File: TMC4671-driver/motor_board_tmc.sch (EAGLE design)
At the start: 135 parts, among them U1 TMC4671-ES, U10 BSC030N08NS5ATMA1, U11 BSC030N08NS5ATMA1, U12 INA28X, U13 INA28X, U14 BSC030N08NS5ATMA1, U15 BSC030N08NS5ATMA1, U16 BSC030N08NS5ATMA1, U17 BSC030N08NS5ATMA1, U18 MCP14XX, U19 BSC030N08NS5ATMA1, U20 BSC030N08NS5ATMA1, U21 BSC030N08NS5ATMA1, U22 NC7NZ17K8X-3-BUFFER, U23 NC7NZ17K8X-3-BUFFER, U3 LM5109BSD, U4 LM5109BSD, U5 LM5109BSD, U6 LM5109BSD, U7 AP3012KTR-G1, U8 LM5050Q1MK-1/NOPB, U9 BSC030N08NS5ATMA1, X1 GMSTBA4, X2 GMSTBA4, X3 2516-, Y1 ECS-327KE-TR

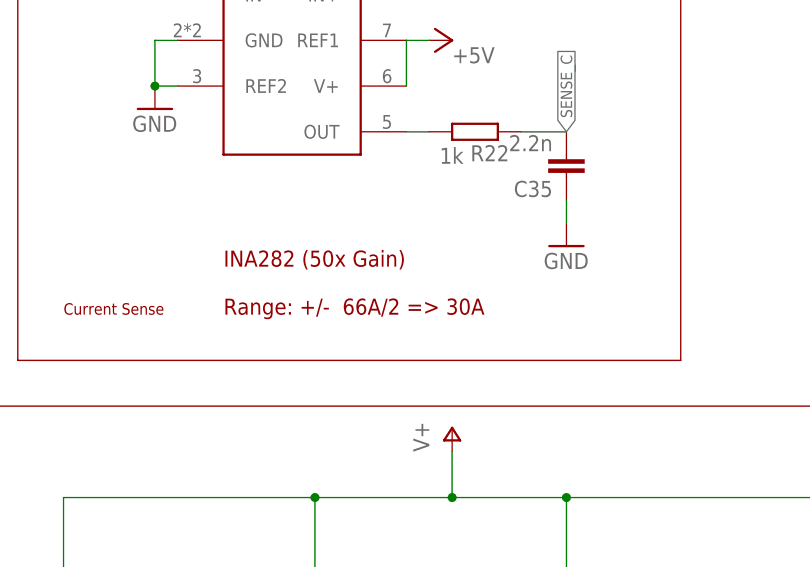
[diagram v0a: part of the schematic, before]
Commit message: Changing clearances to 8 mil and renamed shunt amps
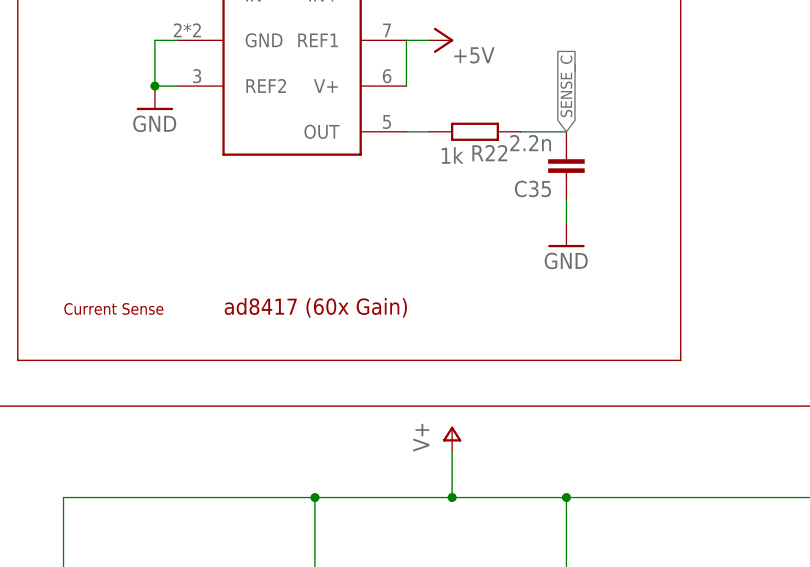
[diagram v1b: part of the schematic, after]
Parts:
- U12, U13: value INA28X -> AD841X; device Powermisc:INA28X -> Powermisc:AD841X
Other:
- note added: "ad8417 (60x Gain)"
- note removed: "INA282 (50x Gain) Range: +/- 66A/2 => 30A"
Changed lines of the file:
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@@
 <part name="R20" library="resistor" library_urn="urn:adsk.eagle:library:348" deviceset="R-EU_" device="R2512" package3d_urn="urn:adsk.eagle:package:23545/2" value="1.5m"/>
 <part name="R19" library="resistor" library_urn="urn:adsk.eagle:library:348" deviceset="R-EU_" device="R2512" package3d_urn="urn:adsk.eagle:package:23545/2" value="1.5m"/>
-<part name="U13" library="Powermisc" deviceset="INA28X" device=""/>
-<part name="U12" library="Powermisc" deviceset="INA28X" device=""/>
+<part name="U13" library="Powermisc" deviceset="AD841X" device=""/>
+<part name="U12" library="Powermisc" deviceset="AD841X" device=""/>
 <part name="P+9" library="supply1" library_urn="urn:adsk.eagle:library:371" deviceset="+5V" device=""/>
 <part name="P+10" library="supply1" library_urn="urn:adsk.eagle:library:371" deviceset="+5V" device=""/>
@@
 <text x="538.48" y="233.68" size="1.27" layer="94">LEDs</text>
 <text x="738.632" y="20.066" size="2.54" layer="94">Connectors</text>
-<text x="292.1" y="160.02" size="1.778" layer="94">INA282 (50x Gain)
-Range: +/-  66A/2 =&gt; 30A</text>
+<text x="292.1" y="160.02" size="1.778" layer="94">ad8417 (60x Gain)
+</text>
 <text x="242.57" y="6.096" size="1.778" layer="94">Shunt Amp Caps</text>
 <wire x1="139.7" y1="27.178" x2="264.16" y2="27.178" width="0.1524" layer="94"/>

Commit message: Updated TMC4671 board to redesigned 1.2 version.
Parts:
- added C42: 100nF, resistor:C-EUC0603
- added C43: 1µF, resistor:C-EUC1206
- added C44: 593D476X0016D2TE3, Powermisc:593D476X0016D2TE3
- added C45: 4.7µF, resistor:C-EUC0805
- added D10: BZX384-XXX, Powermisc:BZX384-XXX
- added D11: HV >100V, adafruit:DIODE_SOD-123FL
- added D12, D14: LV low drop, adafruit:DIODE_SOD-123FL
- added D13: 5.6V zener, adafruit:DIODE_SOD-123FL
- added H5, H6: MOUNT-PAD-ROUND3.0, holes:MOUNT-PAD-ROUND3.0
- added JP11, JP12: (no value), pinhead:PINHD-1X5
- added L2: 10µH, rcl:L-EUL4532P
- added R26, R50: 10k, resistor:R-EU_R0603
- added R41, R42, R43, R44, R45, R46: 1.5k, resistor:R-EU_R0603
- added R47: 294k, resistor:R-EU_R0805
- added R48, R49: 71.5k, resistor:R-EU_R0805
- added SJ4: 3.3V, jumper:SJ
- added U24: AP3012KTR-G1, Powermisc:AP3012KTR-G1
- C10, C17, C18, C19, C7, C9: value 1µF -> 100nF; device resistor:C-EUC1206 -> resistor:C-EUC0603
- C11: value 100µF+ -> 680µF; device resistor:CPOL-EUE5-10.5 -> resistor:CPOL-EUE7.5-16
- C12: value 100nF -> 680µF; device resistor:C-EUC0603 -> resistor:CPOL-EUE7.5-16
- C13, C14, C15: value 100nF -> 1µF; device resistor:C-EUC0603 -> resistor:C-EUC1206
- C16: value 4.7µF -> 1µF; device resistor:C-EUC0805 -> resistor:C-EUC1206
- C20: value 1µF -> 4.7µF; device resistor:C-EUC1206 -> resistor:C-EUC0805
- C21, C22, C24: device resistor:C-EUC0603 -> resistor:C-EUC0805
- C23: value 4.7µF -> 100nF
- C25, C30, C31: value 100nF -> 1n
- C26, C27: device resistor:C-EUC0805 -> resistor:C-EUC0603
- C28: value 100nF -> 4.7µF
- C29: value 100nF -> (none); device resistor:C-EUC0805 -> resistor:CPOL-EUE5-8.5
- C32: value 4.7µF -> 100p; device resistor:C-EUC0805 -> resistor:C-EUC0603
- C33, C35, C37: value 2.2n -> 1n
- C34, C36: value 2.2n -> 100p
- C38, C40: value 2.2n -> 4.7µF; device resistor:C-EUC0603 -> resistor:C-EUC0805
- C39: value 2.2n -> 100nF; device resistor:C-EUC0603 -> resistor:C-EUC0805
- C41: value 2.2n -> 100nF
- C5, C8: value 4.7µF -> 100nF; device resistor:C-EUC0805 -> resistor:C-EUC0603
- C6: value 60µF+ -> 100nF; device resistor:CPOL-EUE5-10.5 -> resistor:C-EUC0603
- D1, D2, D3, D4, D5: device diode:DIODE-SOD123 -> adafruit:DIODE_SOD-123FL
- D6: value LV low drop -> BZX384-XXX; device diode:DIODE-SOD123 -> Powermisc:BZX384-XXX
- D7, D8: value HV >100V -> BZX384-XXX; device diode:DIODE-SOD123 -> Powermisc:BZX384-XXX
- D9: value HV >100V -> LV low drop; device diode:DIODE-SOD123 -> adafruit:DIODE_SOD-123FL
- JP1: device pinhead:PINHD-1X5 -> pinhead:PINHD-1X1
- JP2: device pinhead:PINHD-1X5 -> pinhead:PINHD-2X4
- JP3: device pinhead:PINHD-1X1 -> pinhead:PINHD-2X3
- JP4: device pinhead:PINHD-1X1 -> pinhead:PINHD-1X2
- JP5: value (none) -> 5V; device pinhead:PINHD-1X5 -> jumper:JP1Q
- JP6: device pinhead:PINHD-2X3 -> pinhead:PINHD-1X4
- JP8: device pinhead:PINHD-1X2 -> pinhead:PINHD-2X4
- JP9: device pinhead:PINHD-2X8 -> pinhead:PINHD-2X3
- L1: value 10µH -> 220µH; device rcl:L-EUL4532P -> Powermisc:8MMINDUCTOR
- LED1: value (none) -> Green
- R10, R11, R5, R6, R7, R8, R9: value 10k -> 2.2
- R12: value 33k -> 2.2; device resistor:R-EU_R0805 -> resistor:R-EU_R0603
- R13: value 4.7k -> 71.5k; device resistor:R-EU_R0603 -> resistor:R-EU_R0805
- R14: value 976k -> 1.5k; device resistor:R-EU_R0805 -> resistor:R-EU_R0603
- R15: value 4.7k -> 294k; device resistor:R-EU_R0603 -> resistor:R-EU_R0805
- R16: value 33k -> 10k; device resistor:R-EU_R0805 -> resistor:R-EU_R0603
- R17: value 976k -> 33k
- R18: value 33k -> 294k
- R19: value 1.5m -> 10k; device resistor:R-EU_R2512 -> resistor:R-EU_R0603
- R20: value 1.5m -> 33k; device resistor:R-EU_R2512 -> resistor:R-EU_R0805
- R21, R22: value 1k -> 1.5m; device resistor:R-EU_R0603 -> resistor:R-EU_R2512
- R23: value 10k -> 1.5k
- R24: value 1k -> 1.5k
- R25: value 10k -> 33k; device resistor:R-EU_R0603 -> resistor:R-EU_R0805
- R27, R30, R31: value 4.7k -> 1.5k
- R28: value 4.7k -> 33k; device resistor:R-EU_R0603 -> resistor:R-EU_R0805
- R29: value 4.7k -> 22k thermistor
- R32: value 4.7k -> 10k
- R33: value 330 -> 10k
- R34: value 360k -> 330; device resistor:R-EU_R0805 -> resistor:R-EU_R0603
- R35, R36, R37, R38, R39, R40: value 1k -> 4.7k
- U1: value TMC4671-ES -> TMC4671; device Trinamic:TMC4671-ES -> Trinamic:TMC4671
- U12, U13: value AD841X -> BSC030N08NS5ATMA1; device Powermisc:AD841X -> OHSC_Power:BSC030N08NS5ATMA1
- U14: value BSC030N08NS5ATMA1 -> MCP14XX; device OHSC_Power:BSC030N08NS5ATMA1 -> Powermisc:MCP14XX
- U18: value MCP14XX -> NC7NZ17K8X-3-BUFFER; device Powermisc:MCP14XX -> Powermisc:NC7NZ17K8X-3-BUFFER
- U19: value BSC030N08NS5ATMA1 -> NC7NZ17K8X-3-BUFFER; device OHSC_Power:BSC030N08NS5ATMA1 -> Powermisc:NC7NZ17K8X-3-BUFFER
- U2: value (none) -> LM5109BSD; device SparkFun-IC-Power:V_REG_LM1117SOT223 -> Powermisc:LM5109BSD
- U20: value BSC030N08NS5ATMA1 -> LM74700-Q1; device OHSC_Power:BSC030N08NS5ATMA1 -> OHSC_Power:LM74700-Q1
- U21: value BSC030N08NS5ATMA1 -> (none); device OHSC_Power:BSC030N08NS5ATMA1 -> SparkFun-IC-Power:V_REG_LM1117SOT223
- U22: value NC7NZ17K8X-3-BUFFER -> BSC030N08NS5ATMA1; device Powermisc:NC7NZ17K8X-3-BUFFER -> OHSC_Power:BSC030N08NS5ATMA1
- U23: value NC7NZ17K8X-3-BUFFER -> MAX5033BASA+T; device Powermisc:NC7NZ17K8X-3-BUFFER -> Powermisc:MAX5033BASA+T
- U6: value LM5109BSD -> BSC030N08NS5ATMA1; device Powermisc:LM5109BSD -> OHSC_Power:BSC030N08NS5ATMA1
- U7: value AP3012KTR-G1 -> BSC030N08NS5ATMA1; device Powermisc:AP3012KTR-G1 -> OHSC_Power:BSC030N08NS5ATMA1
- U8: value LM5050Q1MK-1/NOPB -> AD841X; device OHSC_Power:LM5050Q1MK-1/NOPB -> Powermisc:AD841X
- U9: value BSC030N08NS5ATMA1 -> AD841X; device OHSC_Power:BSC030N08NS5ATMA1 -> Powermisc:AD841X
- X1: value GMSTBA4 -> 2516-; device con-phoenix-762:GMSTBA4 -> con-3m:2516-
- X3: value 2516- -> GMSTBA4; device con-3m:2516- -> con-phoenix-762:GMSTBA4
- Y1: value ECS-327KE-TR -> 25MHz
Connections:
- removed net N$14: C28.1, D4.C, U5.HB
- removed net N$26: C26.1, D2.C, U3.HB
- removed net VCORE1: C3.2, U1B.VCCCORE1
- removed net VCORE2: C1.2, U1B.VCCCORE2
- removed net VCORE3: C4.2, U1B.VCCCORE3
- removed net V_ADC/2: R1.1, R2.2, U1A.ADC_I0_NEG, U1A.ADC_I1_NEG, U1A.AENC_UX_NEG, U1A.AENC_VN_NEG, U1A.AENC_WY_NEG
- new net AENC_UX_N: JP2.5, JP3.3, U1A.AENC_UX_NEG
- new net AENC_VN_N: JP2.7, JP3.1, U1A.AENC_VN_NEG
- new net AENC_WY_N: JP2.3, JP3.5, U1A.AENC_WY_NEG
- new net INPUT_GATE: U20.GATE, U22.G
- new net N$16: C42.2, D12.C, L1.1, U23.LX
- new net N$17: R31.2, X1-16.KL
- new net N$19: C42.1, U23.BST
- new net N$20: SJ4.1, X1-4.KL
- new net N$21: R47.1, R48.1, U23.ON/!OFF
- new net N$23: JP5.1, X1-2.KL
- new net N$24: C39.1, U20.VCAP
- new net N$25: C41.2, U23.VD
- new net N$27: R11.2, U5.HO
- new net N$28: C23.1, D4.C, U4.HB
- new net N$29: R10.2, U4.LO
- new net N$30: R9.2, U4.HO
- new net N$31: C21.1, D2.C, U2.HB
- new net N$32: R6.2, U2.LO
- new net N$33: R5.2, U2.HO
- new net N$34: C22.1, D3.C, U3.HB
- new net N$35: R8.2, U3.LO
- new net N$36: R7.2, U3.HO
- new net VCORE: C3.2, C5.2, C6.2, U1B.VCCCORE1, U1B.VCCCORE2, U1B.VCCCORE3
- new net V_SENSE/2: C1.2, C2.2, R1.1, R2.2, U1A.ADC_I0_NEG, U1A.ADC_I1_NEG, U8.REF1, U8.REF2, U9.REF1, U9.REF2
- net +3V3: now also C17.1, C18.1, C19.1, C20.1, C40.1, JP6.4, R29.2, R34.2, SJ4.2, U18.VCC, U19.VCC, U21.OUT, U21.OUT@1; no longer C21.1, C22.1, C24.1, C25.1, C8.1, JP5.5, JP7.2, JP9.2, R33.2, U2.OUT, U2.OUT@1, U22.VCC, U23.VCC, X3-4.KL
- net +5V: now also C26.1, C27.1, C28.1, C29.+, C38.1, C4.2, C44.1, D13.C, JP11.1, JP12.1, JP2.2, JP4.2, JP5.2, L1.2, L2.1, R35.2, R36.2, R37.2, R38.2, R39.2, R40.2, U21.IN, U23.FB, U24.NSHDN, U24.VIN, U8.V+, U9.V+; no longer C16.1, C2.2, C30.1, C31.1, C32.1, C5.1, C6.+, JP1.1, JP2.1, JP5.4, JP8.1, L1.1, R27.2, R28.2, R29.2, R30.2, R31.2, U12.REF1, U12.V+, U13.REF1, U13.V+, U2.IN, U7.NSHDN, U7.VIN, X3-2.KL
- net AENC_UX: now also JP2.6; no longer JP6.1
- net AENC_VN: now also JP2.8; no longer JP6.3
- net AENC_WY: now also JP2.4; no longer JP6.5
- net AGPI_A: now also JP1.1; no longer JP6.2
- net AGPI_B: now also R29.1, R30.2; no longer JP6.4
- net BRAKE_CTRL: now also D9.C, R26.2, R27.2, U14.IN; no longer D6.C, R23.2, R24.2, U18.IN
- net BRAKE_CTRL_EXT: now also R27.1, X1-12.KL; no longer R24.1, X3-12.KL
- net BRAKE_CTRL_TMC: now also D9.A; no longer D6.A
- net BRAKE_GATE: now also U14.OUT, U17.G; no longer U18.OUT, U21.G
- net CS1: now also X1-7.KL; no longer X3-7.KL
- net CS2: now also X1-9.KL; no longer X3-9.KL
- net CS3: now also X1-10.KL; no longer X3-10.KL
- net CS_TMC: no longer JP3.1
- net C_HS_A: now also U5.HI; no longer R7.2, U6.HI
- net C_HS_B: now also U4.HI; no longer R6.2, U5.HI
- net C_HS_C: now also U3.HI; no longer R5.2, U4.HI
- net C_HS_D: now also U2.HI; no longer R4.2, U3.HI
- net C_LS_A: now also U5.LI; no longer R11.2, U6.LI
- net C_LS_B: now also U4.LI; no longer R10.2, U5.LI
- net C_LS_C: now also U3.LI; no longer R9.2, U4.LI
- net C_LS_D: now also U2.LI; no longer R8.2, U3.LI
- net DIR: now also JP10.3; no longer JP9.4
- net ENABLE: now also JP7.2, R31.1; no longer JP7.1, X3-16.KL
- net ENC2_A: now also JP9.2; no longer JP10.1
- net ENC2_B: now also JP9.4; no longer JP10.2
- net ENC2_Z: now also JP9.6; no longer JP10.3
- net ENC_A: now also U18.3Y; no longer U22.3Y
- net ENC_A_5V: now also C36.2, R46.1, U18.3A; no longer C41.2, R40.1, U22.3A
- net ENC_B: now also U18.2Y; no longer U22.2Y
- net ENC_B_5V: now also C34.2, R45.1, U18.2A; no longer C39.2, R39.1, U22.2A
- net ENC_Z: now also U18.1Y; no longer U22.1Y
- net ENC_Z_5V: now also C32.2, R44.1, U18.1A; no longer C40.2, R38.1, U22.1A
- net FLAG: now also D1.C, R4.2, X1-11.KL; no longer D9.C, R25.2, X3-11.KL
- net GND: now also C10.1, C12.-, C13.2, C14.2, C15.2, C26.2, C27.2, C28.2, C29.-, C30.1, C31.1, C32.1, C33.1, C38.2, C40.2, C43.1, C44.2, C45.2, C5.1, C6.1, C7.1, C8.1, C9.1, D12.A, D13.A, H5.MOUNT, H6.MOUNT, JP11.5, JP12.5, JP2.1, JP6.3, JP7.1, R14.1, R17.1, R19.1, R20.1, R26.1, R28.1, R30.1, R33.1, R48.2, R50.1, U13.S, U14.GND, U16.S, U19.GND, U2.EP, U2.VSS, U20.GND, U21.ADJ, U23.SGND, U24.GND, U7.S, U9.GND, X1-1.KL, X2-1.1; no longer C10.2, C12.1, C13.1, C14.1, C15.1, C21.2, C22.2, C23.2, C24.2, C30.2, C31.2, C32.2, C33.2, C38.1, C39.1, C40.1, C5.2, C6.-, C7.2, C8.2, C9.2, D8.A, JP1.5, JP2.5, JP5.3, JP6.6, JP8.2, JP9.1, R10.1, R11.1, R13.1, R15.1, R18.1, R23.1, R5.1, R6.1, R7.1, R8.1, R9.1, U12.GND, U12.REF2, U13.GND, U13.REF2, U15.S, U2.ADJ, U20.S, U21.S, U22.GND, U6.EP, U6.VSS, U7.GND, U8.OFF, X1-1.1, X3-1.KL
- net GPIO0: now also JP8.1; no longer JP9.9
- net GPIO1: now also JP8.2; no longer JP9.10
- net GPIO2: now also JP8.3; no longer JP9.11
- net GPIO3: now also JP8.4; no longer JP9.12
- net GPIO4: now also JP8.5; no longer JP9.13
- net GPIO5: now also JP8.6; no longer JP9.14
- net GPIO6: now also JP8.7; no longer JP9.15
- net GPIO7: now also JP8.8; no longer JP9.16
- net G_HS_A: now also D6.C, R11.1, U6.G; no longer U10.G, U6.HO
- net G_HS_B: now also D7.C, R9.1, U10.G; no longer U14.G, U5.HO
- net G_HS_C: now also D8.C, R7.1, U12.G; no longer U16.G, U4.HO
- net G_HS_D: now also D10.C, R5.1, U15.G; no longer U19.G, U3.HO
- net G_LS_A: now also R12.1, R17.2, U7.G; no longer U11.G, U6.LO
- net G_LS_B: now also R10.1, R20.2, U11.G; no longer U15.G, U5.LO
- net G_LS_C: now also R25.2, R8.1, U13.G; no longer U17.G, U4.LO
- net G_LS_D: now also R28.2, R6.1, U16.G; no longer U20.G, U3.LO
- net HALL_UX: now also U19.3Y; no longer U23.3Y
- net HALL_UX_5V: now also C33.2, R41.1, U19.3A; no longer C37.2, R35.1, U23.3A
- net HALL_V: now also U19.2Y; no longer U23.2Y
- net HALL_V_5V: now also C35.2, R42.1, U19.2A; no longer C36.2, R36.1, U23.2A
- net HALL_WY: now also U19.1Y; no longer U23.1Y
- net HALL_WY_5V: now also C37.2, R43.1, U19.1A; no longer C38.2, R37.1, U23.1A
- net MISO: now also X1-6.KL; no longer X3-6.KL
- net MOSI: now also X1-5.KL; no longer X3-5.KL
- net MOT_A: now also C24.2, D6.A, R22.2, U5.HS, U6.S, U7.D, U8.IN+; no longer C29.2, R20.2, U10.S, U11.D, U12.IN+, U6.HS
- net MOT_A_OUT: now also R22.1, U8.IN-, X3-1.1; no longer R20.1, U12.IN-, X2-1.1
- net MOT_B: now also C23.2, D7.A, U10.S, U11.D, U4.HS, X3-2.1; no longer C28.2, U14.S, U15.D, U5.HS, X2-2.1
- net MOT_C: now also C22.2, D8.A, R21.2, U12.S, U13.D, U3.HS, U9.IN+; no longer C27.2, R19.2, U13.IN+, U16.S, U17.D, U4.HS
- net MOT_C_OUT: now also R21.1, U9.IN-, X3-3.1; no longer R19.1, U13.IN-, X2-3.1
- net MOT_D: now also C21.2, D10.A, U15.S, U16.D, U2.HS, X3-4.1; no longer C26.2, U19.S, U20.D, U3.HS, X2-4.1
- net N$1: now also JP12.4, R37.1, R41.2; no longer JP2.4, R27.1, R35.2
- net N$10: now also R24.2, U9.OUT; no longer R22.2, U13.OUT
- net N$11: now also JP11.2, R35.1, R44.2; no longer JP1.2, R29.1, R38.2
- net N$12: now also D14.A, L2.2, U24.SW; no longer D1.A, L1.2, U7.SW
- net N$13: now also R12.2, U5.LO; no longer U8.GATE, U9.G
- net N$15: now also JP12.2, R40.1, R43.2; no longer JP2.2, R32.1, R37.2
- net N$18: now also C24.1, U5.HB; no longer C29.1, U6.HB
- net N$2: now also X1-15.KL; no longer X3-15.KL
- net N$22: now also JP3.2, JP3.4, JP3.6, R32.1, R33.2; no longer C27.1, D3.C, U4.HB
- net N$3: now also JP12.3, R39.1, R42.2; no longer JP2.3, R31.1, R36.2
- net N$4: now also D1.A; no longer D9.A
- net N$5: now also R49.1, R50.2, U24.FB; no longer R12.1, R13.2, U7.FB
- net N$6: now also R23.2, U8.OUT; no longer R21.2, U12.OUT
- net N$7: now also JP11.4, R38.1, R46.2; no longer JP1.4, R30.1, R40.2
- net N$8: now also R34.1; no longer R33.1
- net N$9: now also JP11.3, R36.1, R45.2; no longer JP1.3, R28.1, R39.2
- net PWM_I: now also JP10.1; no longer JP9.8
- net REF_H: now also JP9.3; no longer JP9.5
- net REF_L: now also JP9.1; no longer JP9.3
- net REF_R: now also JP9.5; no longer JP9.7
- net RESET: now also X1-3.KL; no longer X3-3.KL
- net RES_FET: now also D11.A, U17.D, X2-4.1; no longer D7.A, U21.D, X1-2.1
- net SCK: now also X1-8.KL; no longer X3-8.KL
- net SENSE_A: now also C30.2, R23.1; no longer C34.2, R21.1
- net SENSE_C: now also C31.2, R24.1; no longer C35.2, R22.1
- net STEP: now also JP10.2; no longer JP9.6
- net UART_RX: now also JP6.1; no longer JP5.1
- net UART_TX: now also JP6.2; no longer JP5.2
- net V+: now also C12.+, C13.1, C14.1, C15.1, C16.1, C43.2, D11.C, R13.2, R15.2, R47.2, U12.D, U15.D, U20.CATHODE, U22.D, U23.VIN, U6.D, X2-2.1; no longer C10.1, C17.1, C18.1, C19.1, C20.1, C7.1, C9.1, D7.C, R14.2, R34.2, U14.D, U16.D, U19.D, U8.OUT, U8.VS, U9.D, X1-4.1
- net V_EXT: now also R18.1, R19.2, X1-13.KL; no longer R17.1, R18.2, X3-13.KL
- net V_GD: now also C10.2, C45.1, C7.2, C8.2, C9.2, D14.C, R49.2, U14.VDD, U2.VDD; no longer C12.2, C13.2, C14.2, C15.2, C23.1, D1.C, R12.2, U18.VDD, U6.VDD
- net V_INT: now also R15.1, X1-14.KL; no longer R14.1, X3-14.KL
- net V_INT_TMC: now also C25.1, R13.1, R14.2; no longer C33.1, R15.2, R34.1
- net V_MOT_IN: now also C39.2, R18.2, U20.ANODE, U20.EN, U22.S, X2-3.1; no longer D8.C, R17.2, U8.IN, U9.S, X1-3.1
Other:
- note added: "1.5k - 1n?"
- note added: "5V VM buck"
- note added: "5V fixed!"
- note added: "60V=>1.25V"
- note added: "Analog Encoder"
- note added: "LQH43PN100M26L"
- note added: "Low ESR output cap. See MAX5033 Datasheet for selection info. Must have good input decoupling"
- note added: "Optional filters"
- note added: "Options: 20x gain + 3mOhm = 30A 60x + 1.5mOhm = 20A 60x + 1mOhm = 30A"
- note added: "Sense reference"
- note added: "Single ended jumper"
- note added: "TMC4671-LA"
- note added: "Temperature sense mosfets"
- note added: "Thermistor 22k"
- note added: "Vreg 3.3V"
- note added: "Zeners optional"
- note added: "ad8417 (60x Gain) ad8418 (20x Gain)"
- note added: "https://datasheets.maximintegrated.com/en/ds/MAX5033.pdf MAX5033"
- note removed: "Analog Input"
- note removed: "Enable Jumper"
- note removed: "LV Supply"
- note removed: "Top"
- note removed: "Vreg"
- note removed: "ad8417 (60x Gain)"
- moved on the sheet: C1, C10, C11, C13, C14, C15, C16, C17, C18, C19, C2, C20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

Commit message: Updated TMC Board. Fixed D12 value
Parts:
- added D15: Zener 65V, adafruit:DIODE_SOD-123FL
- D12: value LV low drop -> HV >100V
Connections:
- net GND: now also D15.A
- net RES_FET: now also D15.C
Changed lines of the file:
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@@
 <part name="U23" library="Powermisc" deviceset="MAX5033BASA+T" device=""/>
 <part name="R31" library="resistor" library_urn="urn:adsk.eagle:library:348" deviceset="R-EU_" device="R0603" package3d_urn="urn:adsk.eagle:package:23555/3" value="1.5k"/>
-<part name="D12" library="adafruit" library_urn="urn:adsk.eagle:library:420" deviceset="DIODE" device="_SOD-123FL" package3d_urn="urn:adsk.eagle:package:6240937/1" value="LV low drop"/>
+<part name="D12" library="adafruit" library_urn="urn:adsk.eagle:library:420" deviceset="DIODE" device="_SOD-123FL" package3d_urn="urn:adsk.eagle:package:6240937/1" value="HV &gt;100V"/>
 <part name="P+22" library="supply1" library_urn="urn:adsk.eagle:library:371" deviceset="V+" device=""/>
 <part name="GND43" library="supply1" library_urn="urn:adsk.eagle:library:371" deviceset="GND" device=""/>
@@
 <part name="+3V35" library="supply1" library_urn="urn:adsk.eagle:library:371" deviceset="+3V3" device=""/>
 <part name="C29" library="resistor" library_urn="urn:adsk.eagle:library:348" deviceset="CPOL-EU" device="E5-8.5" package3d_urn="urn:adsk.eagle:package:23374/1"/>
+<part name="D15" library="adafruit" library_urn="urn:adsk.eagle:library:420" deviceset="DIODE" device="_SOD-123FL" package3d_urn="urn:adsk.eagle:package:6240937/1" value="Zener 65V"/>
 </parts>
 <sheets>
@@
 <instance part="U17" gate="G$1" x="365.76" y="58.42" smashed="yes">
 <attribute name="VALUE" x="339.09" y="58.42" size="1.778" layer="96"/>
-<attribute name="NAME" x="369.57" y="60.96" size="1.778" layer="95"/>
+<attribute name="NAME" x="361.95" y="60.96" size="1.778" layer="95"/>
 </instance>
 <instance part="GND28" gate="1" x="368.3" y="45.72" smashed="yes">
@@
 <attribute name="NAME" x="275.463" y="20.8026" size="1.778" layer="95"/>
 <attribute name="VALUE" x="275.463" y="15.7226" size="1.778" layer="96"/>
+</instance>
+<instance part="D15" gate="G$1" x="373.38" y="58.42" smashed="yes" rot="R90">
+<attribute name="NAME" x="375.4374" y="50.8" size="1.778" layer="95" rot="R90"/>
+<attribute name="VALUE" x="378.2314" y="50.8" size="1.778" layer="96" rot="R90"/>
 </instance>
 </instances>
@@
 <pinref part="U17" gate="G$1" pin="S"/>
 <wire x1="368.3" y1="48.26" x2="368.3" y2="53.34" width="0.1524" layer="91"/>
+<wire x1="368.3" y1="53.34" x2="373.38" y2="53.34" width="0.1524" layer="91"/>
+<junction x="368.3" y="53.34"/>
+<pinref part="D15" gate="G$1" pin="A"/>
+<wire x1="373.38" y1="53.34" x2="373.38" y2="55.88" width="0.1524" layer="91"/>
 </segment>
 <segment>
@@
 <junction x="368.3" y="63.5"/>
 <pinref part="D11" gate="G$1" pin="A"/>
-</segment>
-<segment>
+<pinref part="D15" gate="G$1" pin="C"/>
+<wire x1="373.38" y1="60.96" x2="373.38" y2="63.5" width="0.1524" layer="91"/>
+<junction x="373.38" y="63.5"/>
+</segment>
+<segment>

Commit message: Updated crystal capacitor value
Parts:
- added R51: 33k, resistor:R-EU_R0603
- C45: value 4.7µF -> 4.7µF <REMOVE>
- D15: value Zener 65V -> Zener 65V (MMSZ5265BT1G)
- R17, R20, R25, R28: device resistor:R-EU_R0805 -> resistor:R-EU_R0603
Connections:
- net BRAKE_GATE: now also R51.2
- net GND: now also R51.1
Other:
- note added: "non inverting!"
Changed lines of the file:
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@@
 <?xml version="1.0" encoding="utf-8"?>
 <!DOCTYPE eagle SYSTEM "eagle.dtd">
-<eagle version="9.3.1">
+<eagle version="9.6.2">
 <drawing>
 <settings>
@@
 <layer number="91" name="Nets" color="2" fill="1" visible="yes" active="yes"/>
 <layer number="92" name="Busses" color="1" fill="1" visible="yes" active="yes"/>
-<layer number="93" name="Pins" color="2" fill="1" visible="yes" active="yes"/>
+<layer number="93" name="Pins" color="2" fill="1" visible="no" active="yes"/>
 <layer number="94" name="Symbols" color="4" fill="1" visible="yes" active="yes"/>
 <layer number="95" name="Names" color="7" fill="1" visible="yes" active="yes"/>
@@
 <part name="R50" library="resistor" library_urn="urn:adsk.eagle:library:348" deviceset="R-EU_" device="R0603" package3d_urn="urn:adsk.eagle:package:23555/3" value="10k"/>
 <part name="SUPPLY11" library="supply2" library_urn="urn:adsk.eagle:library:372" deviceset="+UB" device=""/>
-<part name="C45" library="resistor" library_urn="urn:adsk.eagle:library:348" deviceset="C-EU" device="C0805" package3d_urn="urn:adsk.eagle:package:23617/2" value="4.7µF"/>
+<part name="C45" library="resistor" library_urn="urn:adsk.eagle:library:348" deviceset="C-EU" device="C0805" package3d_urn="urn:adsk.eagle:package:23617/2" value="4.7µF &lt;REMOVE&gt;"/>
 <part name="L2" library="rcl" library_urn="urn:adsk.eagle:library:334" deviceset="L-EU" device="L4532P" package3d_urn="urn:adsk.eagle:package:23484/1" value="10µH"/>
 <part name="P+4" library="supply1" library_urn="urn:adsk.eagle:library:371" deviceset="V+" device=""/>
@@
 <part name="D8" library="Powermisc" deviceset="BZX384-XXX" device=""/>
 <part name="D10" library="Powermisc" deviceset="BZX384-XXX" device=""/>
-<part name="R17" library="resistor" library_urn="urn:adsk.eagle:library:348" deviceset="R-EU_" device="R0805" package3d_urn="urn:adsk.eagle:package:23553/2" value="33k"/>
-<part name="R20" library="resistor" library_urn="urn:adsk.eagle:library:348" deviceset="R-EU_" device="R0805" package3d_urn="urn:adsk.eagle:package:23553/2" value="33k"/>
-<part name="R25" library="resistor" library_urn="urn:adsk.eagle:library:348" deviceset="R-EU_" device="R0805" package3d_urn="urn:adsk.eagle:package:23553/2" value="33k"/>
-<part name="R28" library="resistor" library_urn="urn:adsk.eagle:library:348" deviceset="R-EU_" device="R0805" package3d_urn="urn:adsk.eagle:package:23553/2" value="33k"/>
+<part name="R17" library="resistor" library_urn="urn:adsk.eagle:library:348" deviceset="R-EU_" device="R0603" package3d_urn="urn:adsk.eagle:package:23555/3" value="33k"/>
+<part name="R20" library="resistor" library_urn="urn:adsk.eagle:library:348" deviceset="R-EU_" device="R0603" package3d_urn="urn:adsk.eagle:package:23555/3" value="33k"/>
+<part name="R25" library="resistor" library_urn="urn:adsk.eagle:library:348" deviceset="R-EU_" device="R0603" package3d_urn="urn:adsk.eagle:package:23555/3" value="33k"/>
+<part name="R28" library="resistor" library_urn="urn:adsk.eagle:library:348" deviceset="R-EU_" device="R0603" package3d_urn="urn:adsk.eagle:package:23555/3" value="33k"/>
 <part name="L1" library="Powermisc" deviceset="8MMINDUCTOR" device="" package3d_urn="urn:adsk.eagle:package:15122/1" value="220µH"/>
 <part name="P+23" library="supply1" library_urn="urn:adsk.eagle:library:371" deviceset="+5V" device=""/>
@@
 <part name="+3V35" library="supply1" library_urn="urn:adsk.eagle:library:371" deviceset="+3V3" device=""/>
 <part name="C29" library="resistor" library_urn="urn:adsk.eagle:library:348" deviceset="CPOL-EU" device="E5-8.5" package3d_urn="urn:adsk.eagle:package:23374/1"/>
-<part name="D15" library="adafruit" library_urn="urn:adsk.eagle:library:420" deviceset="DIODE" device="_SOD-123FL" package3d_urn="urn:adsk.eagle:package:6240937/1" value="Zener 65V"/>
+<part name="D15" library="adafruit" library_urn="urn:adsk.eagle:library:420" deviceset="DIODE" device="_SOD-123FL" package3d_urn="urn:adsk.eagle:package:6240937/1" value="Zener 65V (MMSZ5265BT1G)"/>
+<part name="R51" library="resistor" library_urn="urn:adsk.eagle:library:348" deviceset="R-EU_" device="R0603" package3d_urn="urn:adsk.eagle:package:23555/3" value="33k"/>
 </parts>
 <sheets>
@@
 <text x="256.54" y="144.78" size="1.778" layer="97">Zeners optional</text>
 <text x="81.28" y="172.72" size="1.778" layer="97">TMC4671-LA</text>
+<text x="339.09" y="75.692" size="1.778" layer="97">non inverting!</text>
 </plain>
 <instances>
@@
 </instance>
 <instance part="C24" gate="G$1" x="236.22" y="139.7" smashed="yes">
-<attribute name="NAME" x="240.284" y="140.081" size="1.778" layer="95"/>
-<attribute name="VALUE" x="240.284" y="137.541" size="1.778" layer="96"/>
+<attribute name="NAME" x="245.364" y="140.081" size="1.778" layer="95"/>
+<attribute name="VALUE" x="237.744" y="140.081" size="1.778" layer="96"/>
 </instance>
 <instance part="SUPPLY4" gate="G$1" x="170.18" y="147.32" smashed="yes">
@@
 <attribute name="VALUE" x="378.2314" y="50.8" size="1.778" layer="96" rot="R90"/>
 </instance>
+<instance part="R51" gate="G$1" x="360.68" y="50.8" smashed="yes" rot="R90">
+<attribute name="NAME" x="359.1814" y="46.99" size="1.778" layer="95" rot="R90"/>
+<attribute name="VALUE" x="363.982" y="46.99" size="1.778" layer="96" rot="R90"/>
+</instance>
 </instances>
 <busses>
@@
 <pinref part="D15" gate="G$1" pin="A"/>
 <wire x1="373.38" y1="53.34" x2="373.38" y2="55.88" width="0.1524" layer="91"/>
+<pinref part="R51" gate="G$1" pin="1"/>
+<wire x1="360.68" y1="45.72" x2="365.76" y2="45.72" width="0.1524" layer="91"/>
+<wire x1="365.76" y1="45.72" x2="365.76" y2="48.26" width="0.1524" layer="91"/>
+<wire x1="365.76" y1="48.26" x2="368.3" y2="48.26" width="0.1524" layer="91"/>
+<junction x="368.3" y="48.26"/>
 </segment>
 <segment>
@@
 <pinref part="U14" gate="G$1" pin="OUT"/>
 <wire x1="358.14" y1="71.12" x2="360.68" y2="71.12" width="0.1524" layer="91"/>
+<pinref part="R51" gate="G$1" pin="2"/>
 </segment>
 </net>
